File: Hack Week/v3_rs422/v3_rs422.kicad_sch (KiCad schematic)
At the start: 3 parts, among them J1 DE9_Socket, J2 Conn_01x04_Socket, U1 MAX3490xSA

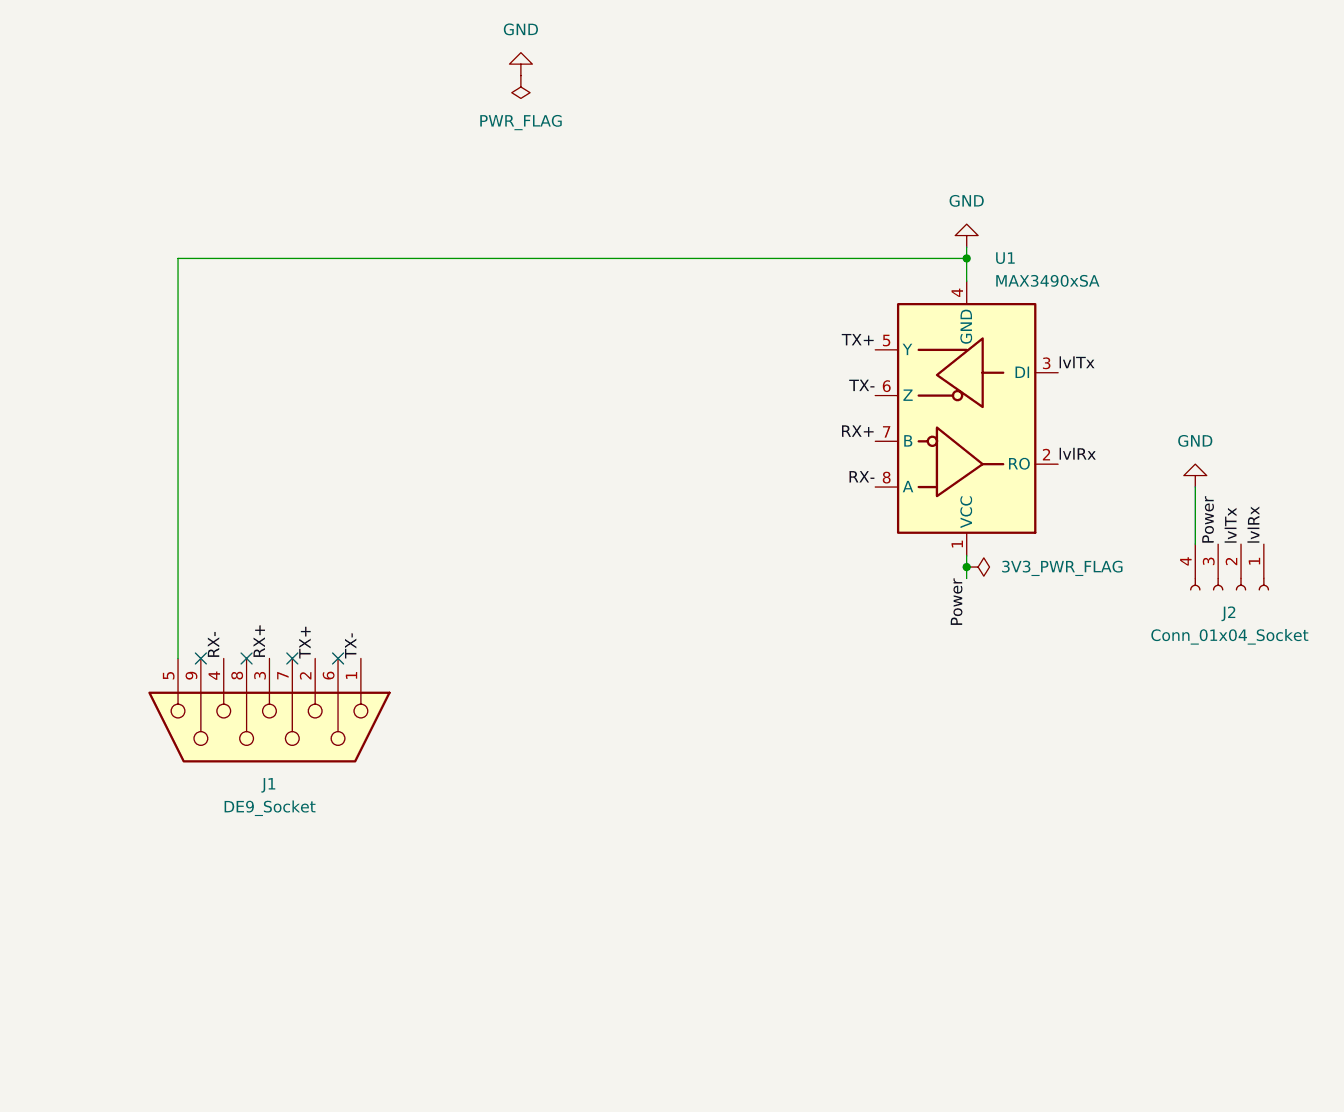
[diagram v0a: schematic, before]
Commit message: changed DB9 connectors + added RS485
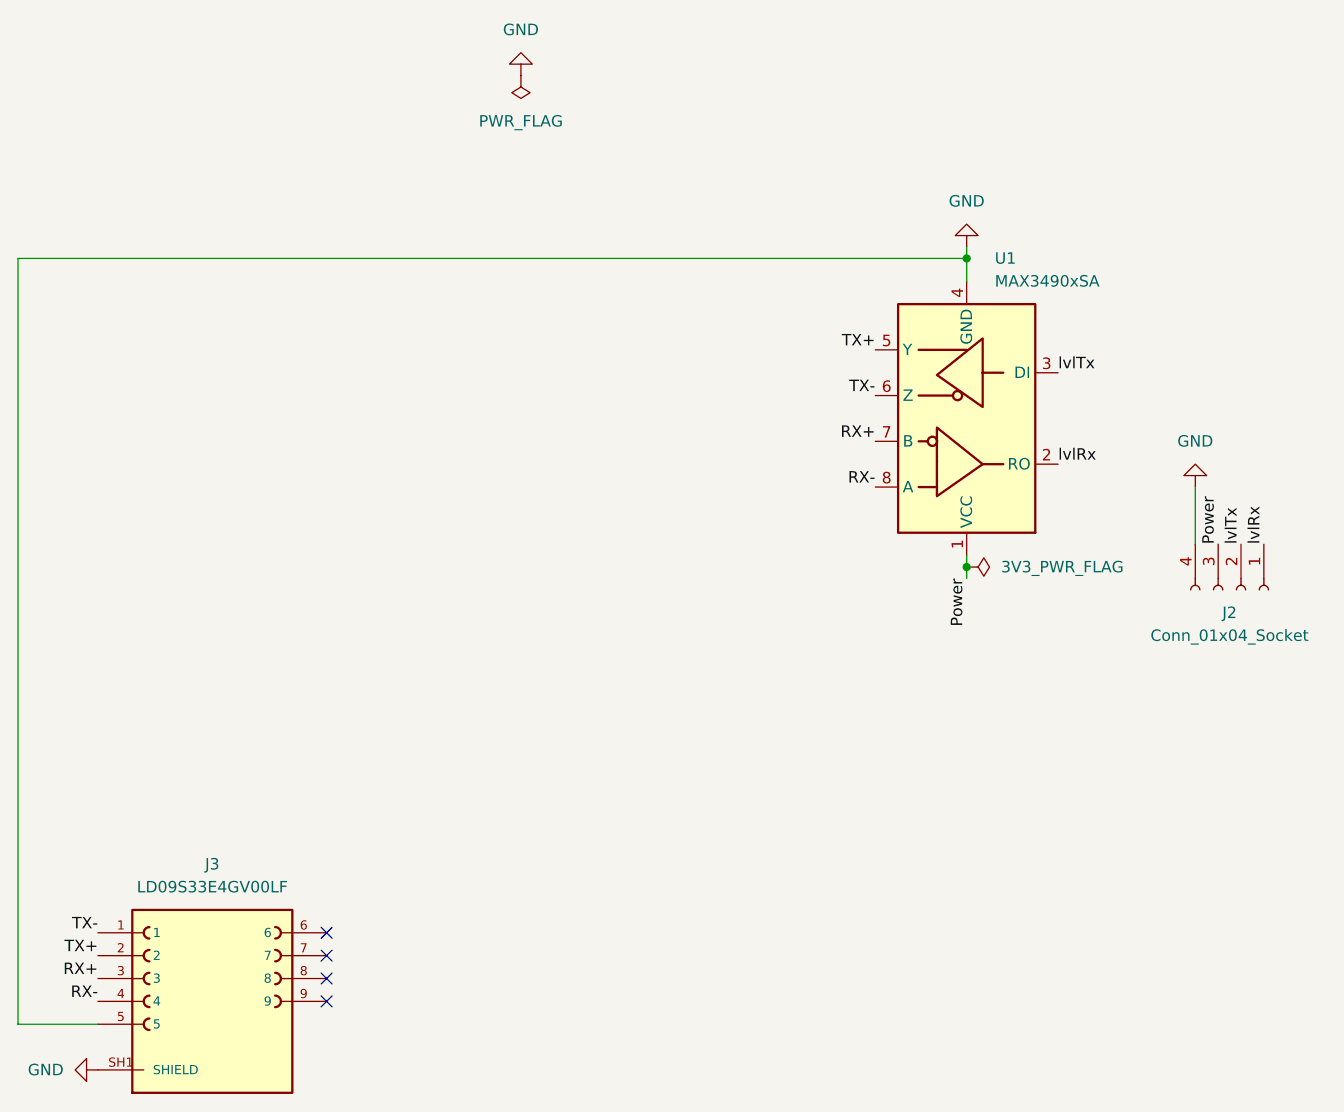
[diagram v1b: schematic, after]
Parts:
- removed J1: DE9_Socket, Connector_Dsub:DSUB-9_Socket_EdgeMount_P2.77mm, symbol Connector:DE9_Socket
- added J3: LD09S33E4GV00LF, Connector_Pin:AMPHENOL_LD09S33E4GV00LF, symbol LD09S33E4GV00LF:LD09S33E4GV00LF
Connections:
- net GND: now also J3.5, J3.SH1 (SHIELD), J3.SH2 (SHIELD)
- net RX+: now also J3.3
- net RX-: now also J3.4
- net TX+: now also J3.2
- net TX-: now also J3.1
